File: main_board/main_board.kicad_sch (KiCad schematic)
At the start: 10 parts

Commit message: Rev 1 draft
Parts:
- removed C18, C9: 100n, Capacitor_SMD:C_0805_2012Metric_Pad1.18x1.45mm_HandSolder, symbol Device:C
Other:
- sheet Battery management ports: added none; removed USBC_MX1_USB2_N, USBC_MX1_USB2_P
- sheet CM5_GPIO ports: added none; removed CM5_PMIC_EN
- sheet CM5_HighSpeed ports: added KB_SCL, KB_SDA; removed USB2_N, USB2_P
- note added: "Connectors ------- HDMI CSI/DSI USB Input per. conn"
- note removed: "Connectors ------- HDMI CSI/DSI USB"
- note removed: "Probably should be close to CM5"

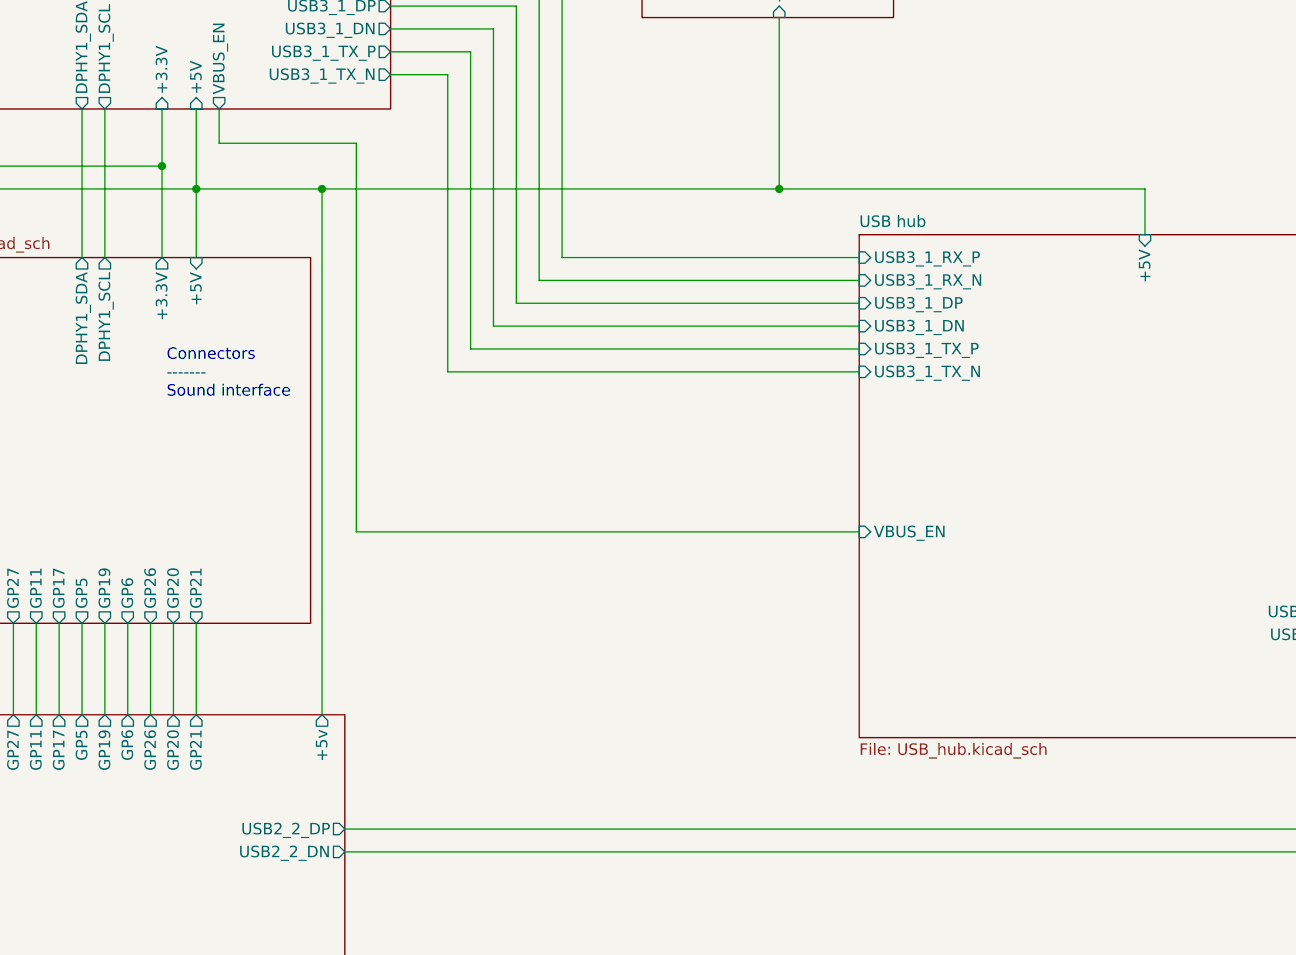
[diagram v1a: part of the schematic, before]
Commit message: Remove passives from hub
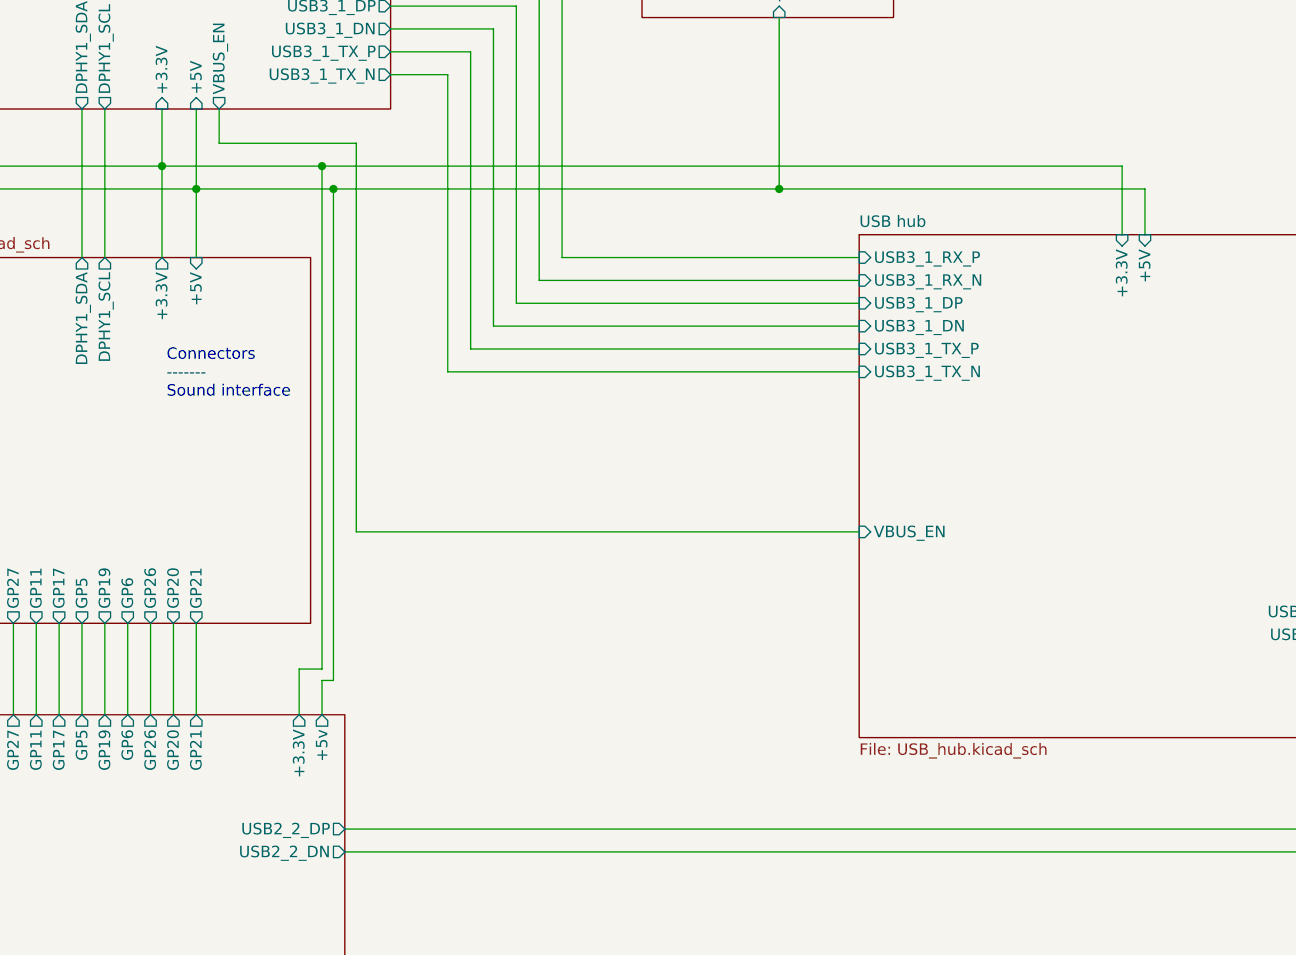
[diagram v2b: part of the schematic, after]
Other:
- sheet The card ports: added +3.3V; removed none
- sheet USB hub ports: added +3.3V; removed none
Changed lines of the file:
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@@
+	)
+	(junction
+		(at 148.59 87.63)
+		(diameter 0)
+		(color 0 0 0 0)
 	)
 	(junction
@@
 	)
 	(junction
+		(at 149.86 90.17)
+		(diameter 0)
+		(color 0 0 0 0)
+	)
+	(junction
 		(at 87.63 45.72)
 		(diameter 0)
@@
 		(color 0 0 0 0)
 	)
-	(junction
-		(at 148.59 90.17)
-		(diameter 0)
-		(color 0 0 0 0)
+	(wire
+		(pts
+			(xy 148.59 87.63) (xy 148.59 143.51)
+		)
+		(stroke
+			(width 0)
+			(type default)
+		)
 	)
 	(wire
@@
 	(wire
 		(pts
+			(xy 148.59 148.59) (xy 148.59 144.78)
+		)
+		(stroke
+			(width 0)
+			(type default)
+		)
+	)
+	(wire
+		(pts
 			(xy 80.01 90.17) (xy 134.62 90.17)
 		)
@@
 	(wire
 		(pts
+			(xy 148.59 144.78) (xy 149.86 144.78)
+		)
+		(stroke
+			(width 0)
+			(type default)
+		)
+	)
+	(wire
+		(pts
 			(xy 124.46 138.43) (xy 124.46 148.59)
 		)
@@
 	(wire
 		(pts
+			(xy 130.81 81.28) (xy 130.81 87.63)
+		)
+		(stroke
+			(width 0)
+			(type default)
+		)
+	)
+	(wire
+		(pts
 			(xy 124.46 81.28) (xy 124.46 97.79)
 		)
@@
 	(wire
 		(pts
+			(xy 146.05 148.59) (xy 146.05 143.51)
+		)
+		(stroke
+			(width 0)
+			(type default)
+		)
+	)
+	(wire
+		(pts
 			(xy 199.39 71.12) (xy 199.39 90.17)
 		)
@@
 	(wire
 		(pts
+			(xy 237.49 95.25) (xy 237.49 87.63)
+		)
+		(stroke
+			(width 0)
+			(type default)
+		)
+	)
+	(wire
+		(pts
 			(xy 165.1 107.95) (xy 165.1 74.93)
 		)
@@
 	(wire
 		(pts
+			(xy 146.05 143.51) (xy 148.59 143.51)
+		)
+		(stroke
+			(width 0)
+			(type default)
+		)
+	)
+	(wire
+		(pts
 			(xy 175.26 97.79) (xy 175.26 64.77)
 		)
@@
 	(wire
 		(pts
+			(xy 148.59 87.63) (xy 237.49 87.63)
+		)
+		(stroke
+			(width 0)
+			(type default)
+		)
+	)
+	(wire
+		(pts
 			(xy 87.63 115.57) (xy 96.52 115.57)
 		)
@@
 	(wire
 		(pts
-			(xy 148.59 90.17) (xy 148.59 148.59)
+			(xy 149.86 90.17) (xy 149.86 144.78)
 		)
 		(stroke
@@
 	(wire
 		(pts
+			(xy 130.81 87.63) (xy 148.59 87.63)
+		)
+		(stroke
+			(width 0)
+			(type default)
+		)
+	)
+	(wire
+		(pts
 			(xy 152.4 128.27) (xy 208.28 128.27)
 		)
@@
 	(wire
 		(pts
-			(xy 148.59 90.17) (xy 199.39 90.17)
-		)
-		(stroke
-			(width 0)
-			(type default)
-		)
-	)
-	(wire
-		(pts
 			(xy 114.3 138.43) (xy 114.3 148.59)
 		)
@@
 	(wire
 		(pts
-			(xy 134.62 90.17) (xy 148.59 90.17)
+			(xy 134.62 90.17) (xy 149.86 90.17)
 		)
 		(stroke
@@
 	(wire
 		(pts
+			(xy 149.86 90.17) (xy 199.39 90.17)
+		)
+		(stroke
+			(width 0)
+			(type default)
+		)
+	)
+	(wire
+		(pts
 			(xy 156.21 60.96) (xy 184.15 60.96)
 		)
@@
 		(pts
 			(xy 240.03 90.17) (xy 199.39 90.17)
-		)
-		(stroke
-			(width 0)
-			(type default)
-		)
-	)
-	(wire
-		(pts
-			(xy 130.81 81.28) (xy 130.81 87.63)
 		)
 		(stroke
@@
 			)
 		)
+		(pin "+3.3V" output
+			(at 146.05 148.59 90)
+			(effects
+				(font
+					(size 1.27 1.27)
+				)
+				(justify right)
+			)
+		)
 		(instances
 			(project "main_board"
@@
 			)
 		)
+		(pin "+3.3V" input
+			(at 237.49 95.25 90)
+			(effects
+				(font
+					(size 1.27 1.27)
+				)
+				(justify right)
+			)
+		)

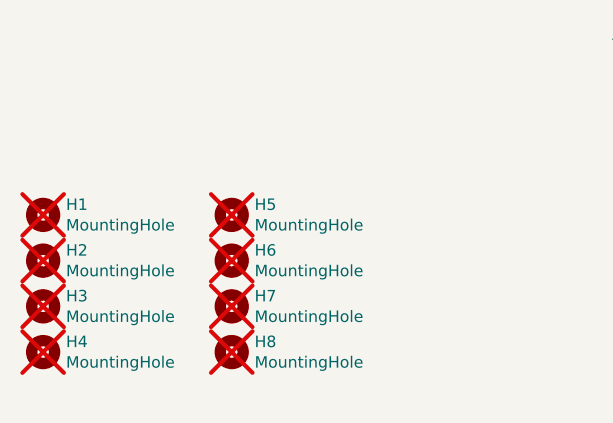
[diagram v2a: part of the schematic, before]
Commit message: Make sure, that audio jack can be hand soldered, finalize rev 1 design.
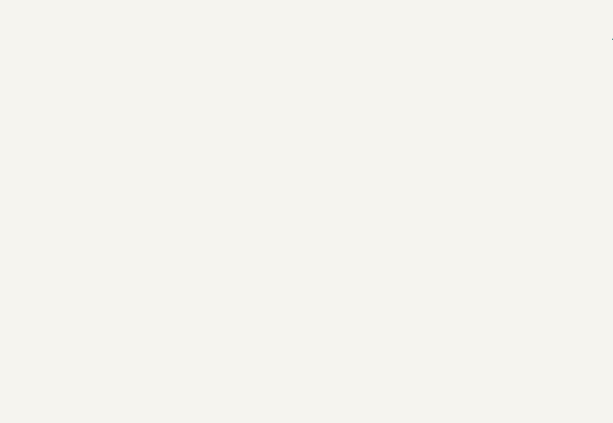
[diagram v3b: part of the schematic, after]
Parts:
- removed H1, H2, H3, H4, H5, H6, H7, H8: MountingHole, CM5IO:MountingHole_2.7mm_M2.5_DIN965, symbol Mechanical:MountingHole

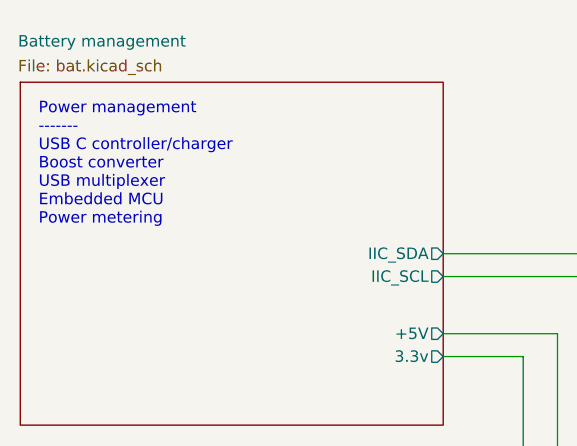
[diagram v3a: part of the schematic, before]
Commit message: Fix bad output voltage
For some reason I got 5V with previous values on prototype. Weird...
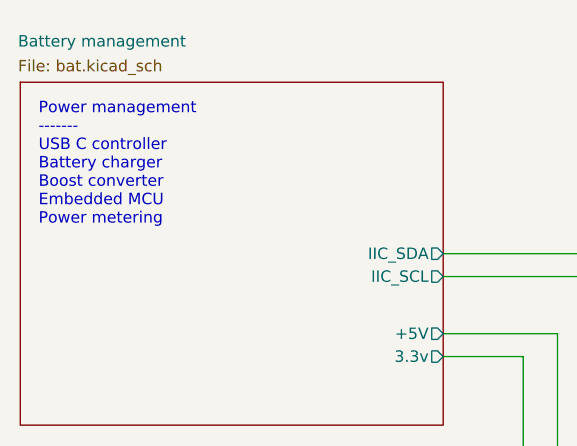
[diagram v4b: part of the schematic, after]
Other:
- note added: "Power management ------- USB C controller Battery charger Boost converter Embedded MCU Power metering"
- note removed: "Power management ------- USB C controller/charger Boost converter USB multiplexer Embedded MCU Power metering"
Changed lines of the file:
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@@
 		)
 	)
-	(text "Power management\n-------\nUSB C controller/charger\nBoost converter\nUSB multiplexer\nEmbedded MCU\nPower metering\n"
+	(text "Power management\n-------\nUSB C controller\nBattery charger\nBoost converter\nEmbedded MCU\nPower metering\n"
 		(exclude_from_sim no)
 		(at 22.352 36.322 0)

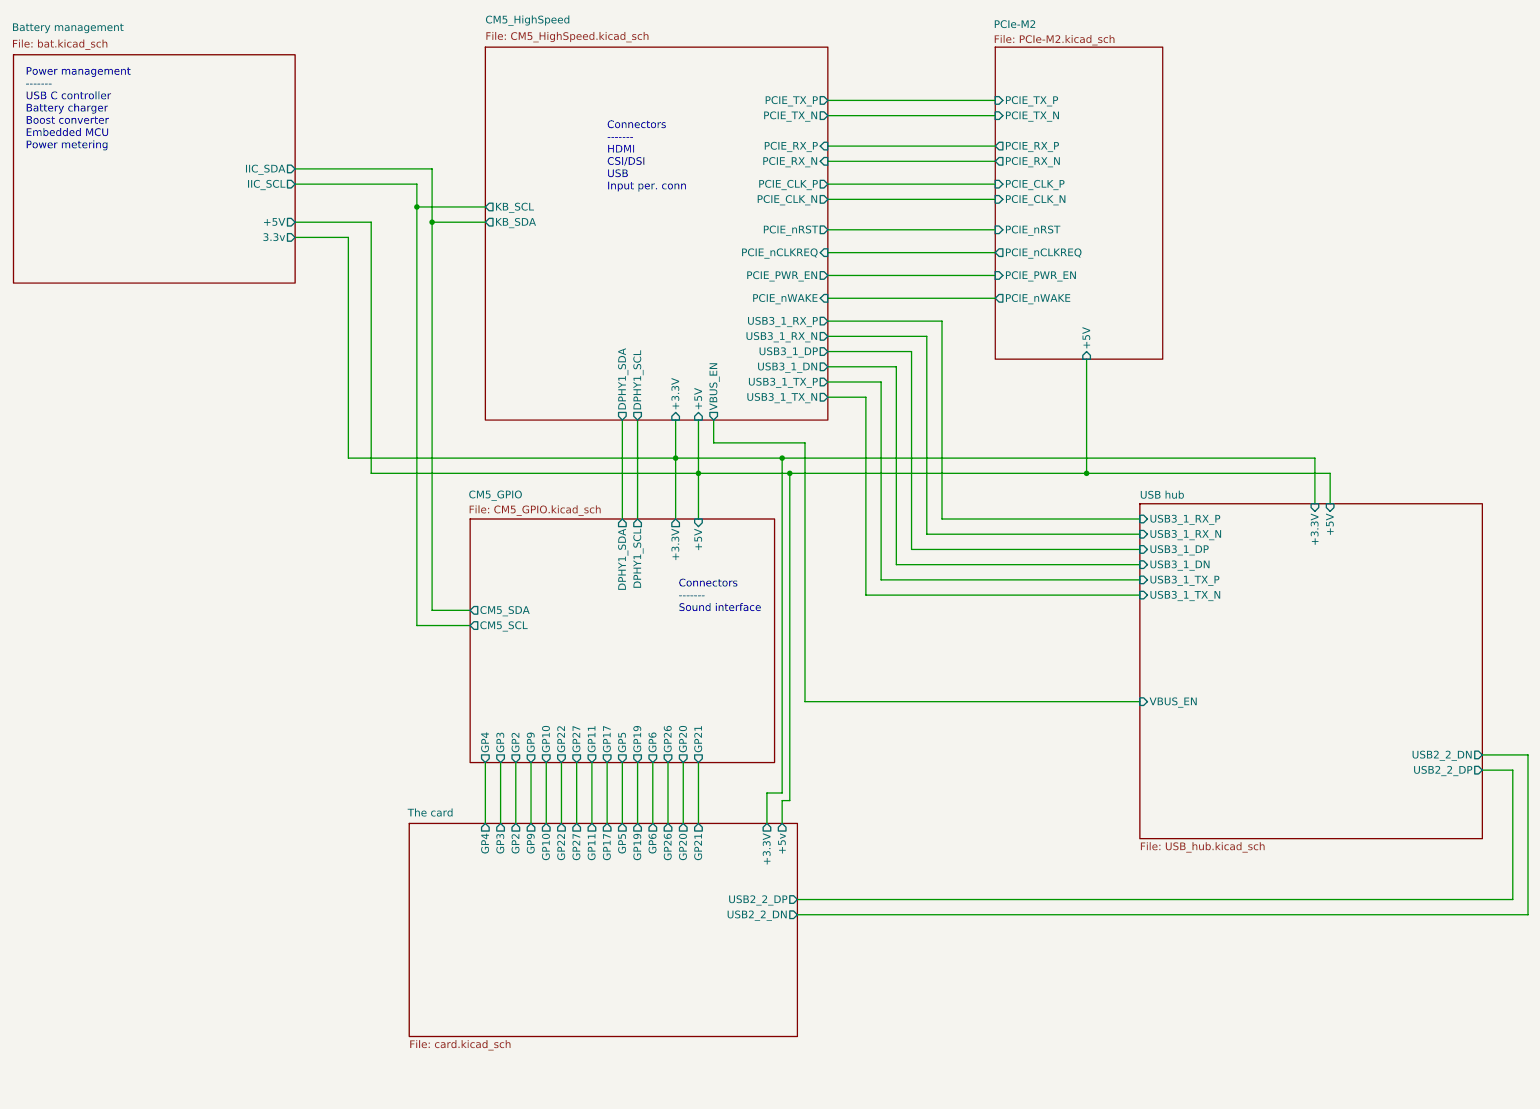
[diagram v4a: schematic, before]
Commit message: Fix critical problems
- Adding USB2 hub on USB3 port did not work correctly
- PM I2C bus was not working when CM5 is shut down
- Missing OTG ID pin
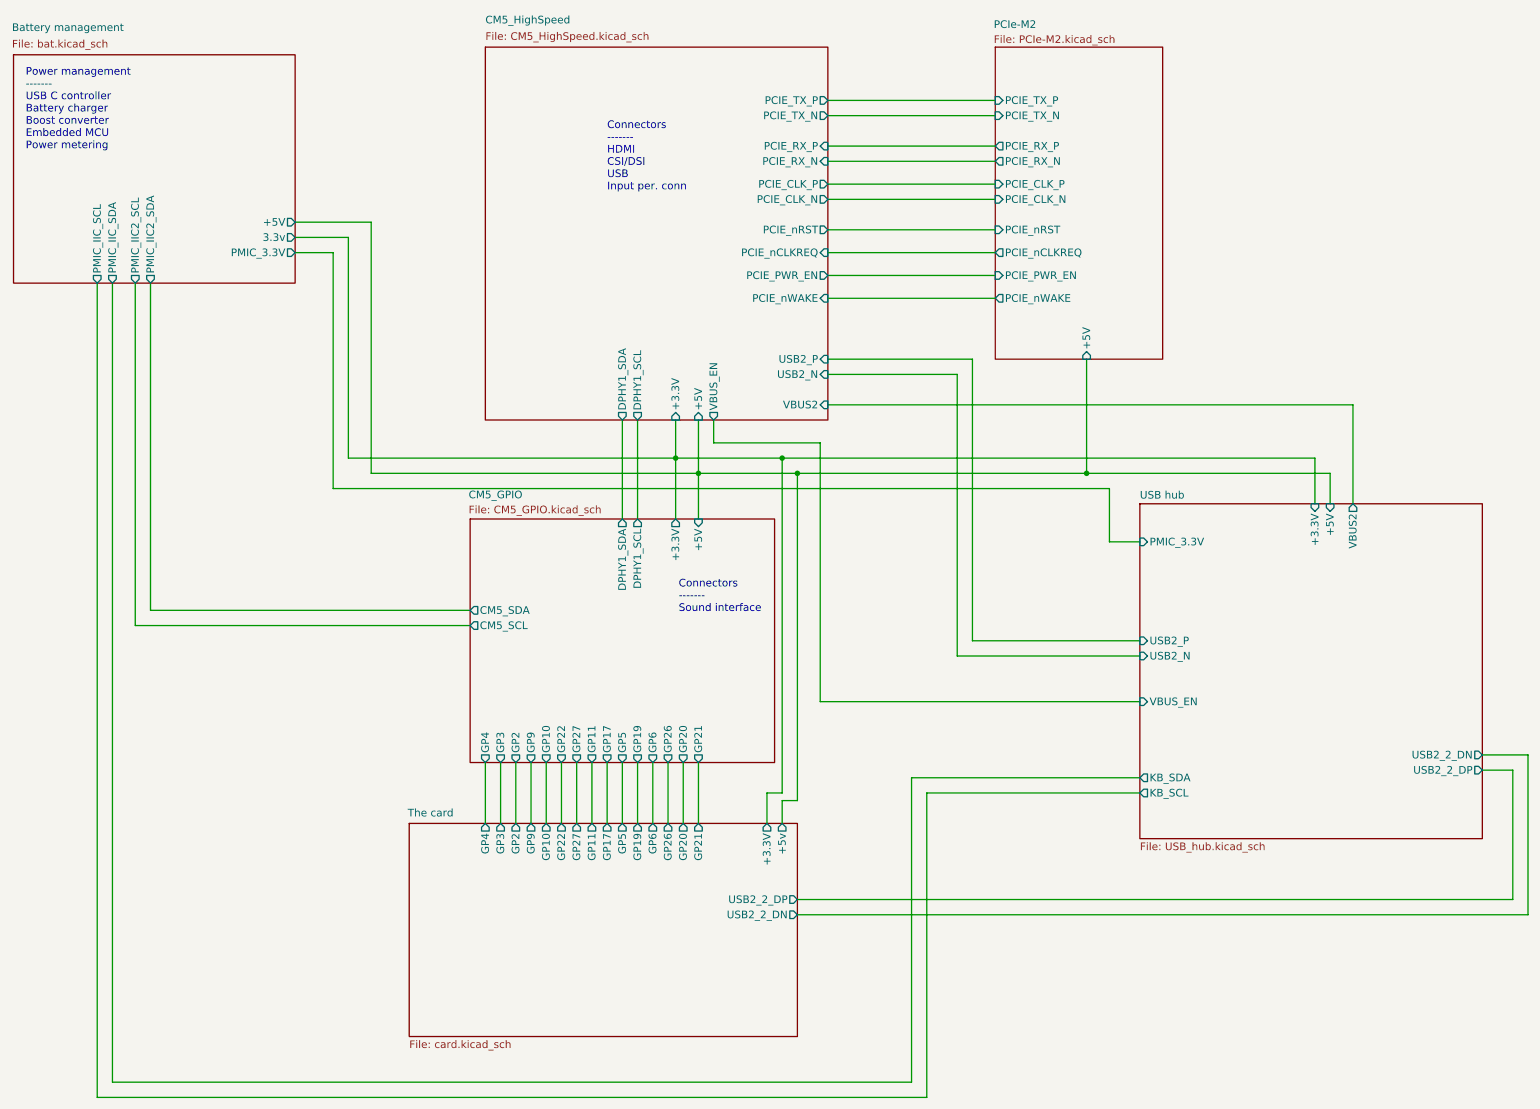
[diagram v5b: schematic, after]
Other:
- sheet Battery management ports: added PMIC_3.3V, PMIC_IIC2_SCL, PMIC_IIC2_SDA, PMIC_IIC_SCL, PMIC_IIC_SDA; removed IIC_SCL, IIC_SDA
- sheet CM5_HighSpeed ports: added USB2_N, USB2_P, VBUS2; removed KB_SCL, KB_SDA, USB3_1_DN, USB3_1_DP, USB3_1_RX_N, USB3_1_RX_P, USB3_1_TX_N, USB3_1_TX_P
- sheet USB hub ports: added KB_SCL, KB_SDA, PMIC_3.3V, USB2_N, USB2_P, VBUS2; removed USB3_1_DN, USB3_1_DP, USB3_1_RX_N, USB3_1_RX_P, USB3_1_TX_N, USB3_1_TX_P

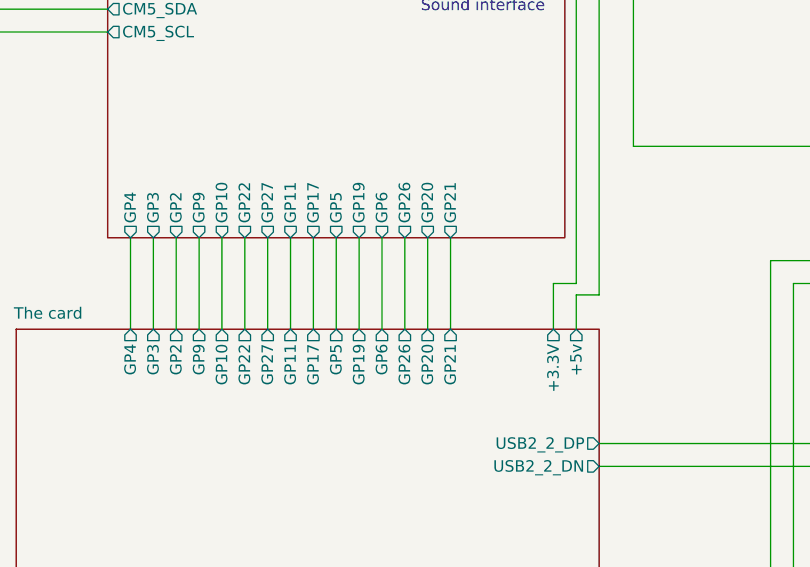
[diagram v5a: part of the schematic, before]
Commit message: Use I2S sound chip instead of PWM output
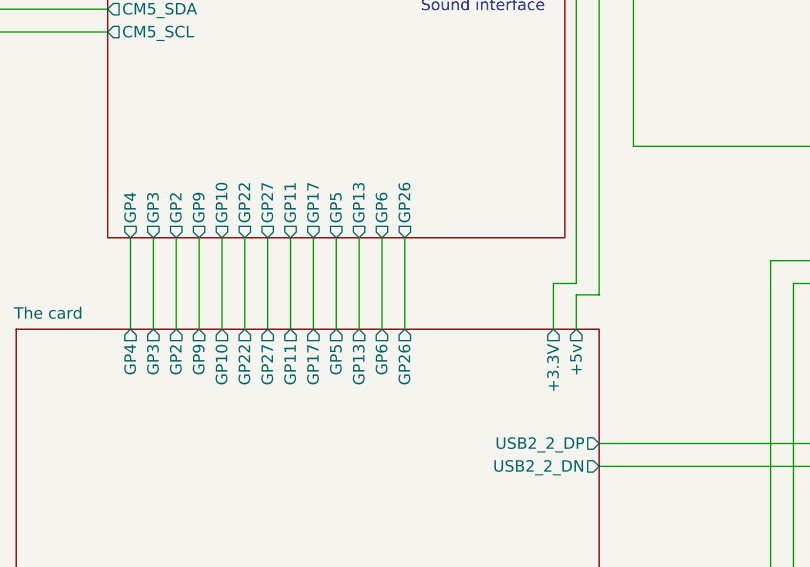
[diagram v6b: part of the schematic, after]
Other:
- sheet CM5_GPIO ports: added GP13; removed GP19, GP20, GP21
- sheet The card ports: added GP13; removed GP19, GP20, GP21
